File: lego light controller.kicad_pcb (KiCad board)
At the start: 2 copper layers, 31.8 x 31.8 mm, 29 parts, among them J1 Conn_01x02, J2 Conn_01x02, J3 Conn_01x02, J4 Conn_01x03, J5 Conn_01x03, J7 Conn_01x06_Pin, P1 USB_C_Plug_USB2.0, Q1 BC847W, Q2 BC847W, Q3 BC847W, U1 ATSAMD11C14A-SS, U2 AMS1117-3.3

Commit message: clean up pcb
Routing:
- net GND: track 2.35 -> 0.84 mm
- net /USB_N: track 12.6 -> 11.2 mm
- net /USB_P: track 9.55 -> 8.87 mm
- net Net-(J3-Pin_2): track 2.72 -> 2.09 mm
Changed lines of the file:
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@@
         (effects (font (size 1 1) (thickness 0.15)) (justify mirror))
     )
-    (fp_text value "10k" (at 0 1.43 90) (layer "F.Fab")
+    (fp_text value "10k" (at 0 1.43 90) (layer "F.Fab") hide
         (effects (font (size 1 1) (thickness 0.15)))
     )
@@
         (effects (font (size 1 1) (thickness 0.15)) (justify mirror))
     )
-    (fp_text value "1k" (at 0 1.43 90) (layer "F.Fab")
+    (fp_text value "1k" (at 0 1.43 90) (layer "F.Fab") hide
         (effects (font (size 1 1) (thickness 0.15)))
     )
@@
         (effects (font (size 1 1) (thickness 0.15)) (justify mirror))
     )
-    (fp_text value "100n" (at 40.94 0.35 90) (layer "F.Fab")
+    (fp_text value "100n" (at 40.94 0.35 90) (layer "F.Fab") hide
         (effects (font (size 1 1) (thickness 0.15)))
     )
@@
     (property "ki_keywords" "R res resistor")
     (attr smd)
-    (fp_text reference "R12" (at 2.2 0.15) (layer "B.SilkS")
+    (fp_text reference "R12" (at 1.95 1.15) (layer "B.SilkS")
         (effects (font (size 1 1) (thickness 0.15)) (justify mirror))
     )
@@
   )
   (segment (start 186 88.62) (end 186 89.465) (width 0.25) (layer "F.Cu") (net 1))
-  (segment (start 186 89.465) (end 185.625 89.84) (width 0.25) (layer "F.Cu") (net 1))
   (via (at 204.3 87.3) (size 0.8) (drill 0.4) (layers "F.Cu" "B.Cu") (free) (net 1))
   (via (at 194.7 89.9) (size 0.8) (drill 0.4) (layers "F.Cu" "B.Cu") (free) (net 1))
@@
   (via (at 187.2 84.6) (size 0.8) (drill 0.4) (layers "F.Cu" "B.Cu") (free) (net 1))
   (via (at 181.3 95.2) (size 0.8) (drill 0.4) (layers "F.Cu" "B.Cu") (free) (net 1))
-  (segment (start 185.771142 80.698712) (end 185.771142 81.671142) (width 0.25) (layer "B.Cu") (net 1))
   (segment (start 195.05 87.85) (end 195.27 87.63) (width 0.25) (layer "F.Cu") (net 2))
   (segment (start 188.45 88.9) (end 191.15 88.9) (width 0.25) (layer "F.Cu") (net 2))
   (segment (start 195.9 87.8) (end 195.85 87.85) (width 0.25) (layer "F.Cu") (net 2))
-  (segment (start 188.4 88.85) (end 188.45 88.9) (width 0.25) (layer "F.Cu") (net 2))
   (segment (start 190.1 92.2) (end 188.4 90.5) (width 0.25) (layer "F.Cu") (net 2))
   (segment (start 191.35 88.7) (end 194.2 88.7) (width 0.25) (layer "F.Cu") (net 2))
@@
   (segment (start 185.329594 87.87) (end 185.179594 87.72) (width 0.25) (layer "F.Cu") (net 3))
   (segment (start 185.4 83.05) (end 185.9 83.05) (width 0.25) (layer "F.Cu") (net 3))
-  (segment (start 185.9 87.75) (end 185.78 87.87) (width 0.25) (layer "F.Cu") (net 3))
   (segment (start 183.7 87.9) (end 183.7 84.75) (width 0.25) (layer "F.Cu") (net 3))
   (segment (start 190.7 96.7) (end 191.45 95.95) (width 0.5) (layer "F.Cu") (net 3))
   (segment (start 209.975 88) (end 208.475 86.5) (width 0.5) (layer "F.Cu") (net 3))
   (segment (start 209.5 96.7) (end 209.975 96.225) (width 0.5) (layer "F.Cu") (net 3))
-  (segment (start 204.96 84.94) (end 205.02 85) (width 0.5) (layer "B.Cu") (net 3))
   (segment (start 204.96 81.8) (end 204.96 84.94) (width 0.5) (layer "B.Cu") (net 3))
   (segment (start 205.1 89.2) (end 206.335 89.2) (width 0.25) (layer "F.Cu") (net 4))
   (segment (start 206.335 89.2) (end 207.535 88) (width 0.25) (layer "F.Cu") (net 4))
-  (segment (start 205 89.1) (end 205.1 89.2) (width 0.25) (layer "F.Cu") (net 4))
   (segment (start 205.05 91.8) (end 206.735 91.8) (width 0.25) (layer "F.Cu") (net 5))
-  (segment (start 205 91.75) (end 205.05 91.8) (width 0.25) (layer "F.Cu") (net 5))
   (segment (start 206.735 91.8) (end 207.535 91) (width 0.25) (layer "F.Cu") (net 5))
-  (segment (start 207.085 94.45) (end 207.535 94) (width 0.25) (layer "F.Cu") (net 6))
   (segment (start 205 94.45) (end 207.085 94.45) (width 0.25) (layer "F.Cu") (net 6))
   (segment (start 203.725 83.6) (end 206.16 83.6) (width 0.25) (layer "F.Cu") (net 7))
@@
   (segment (start 186 83.77) (end 187.43 83.77) (width 0.25) (layer "F.Cu") (net 10))
   (segment (start 187.43 83.77) (end 188.655 82.545) (width 0.25) (layer "F.Cu") (net 10))
-  (segment (start 188.655 82.545) (end 188.655 82.32) (width 0.25) (layer "F.Cu") (net 10))
   (segment (start 202.1 88) (end 202.1 90.6) (width 0.25) (layer "F.Cu") (net 11))
   (segment (start 201.525 87.425) (end 202.1 88) (width 0.25) (layer "F.Cu") (net 11))
@@
   (segment (start 185.43 91.87) (end 186.465 91.87) (width 0.25) (layer "F.Cu") (net 12))
   (segment (start 185.3 92) (end 185.43 91.87) (width 0.25) (layer "F.Cu") (net 12))
-  (segment (start 186.465 91.87) (end 186.465 91.635) (width 0.25) (layer "F.Cu") (net 12))
   (segment (start 185.974975 86.744975) (end 186 86.77) (width 0.25) (layer "F.Cu") (net 12))
   (via (at 184.555025 86.744975) (size 0.8) (drill 0.4) (layers "F.Cu" "B.Cu") (net 12))
@@
   (segment (start 189.774695 81.8) (end 196.195 81.8) (width 0.25) (layer "B.Cu") (net 23))
   (segment (start 190.19 87.6) (end 189.275 86.685) (width 0.25) (layer "B.Cu") (net 23))
-  (segment (start 186 86.27) (end 186.735 86.27) (width 0.2) (layer "F.Cu") (net 25))
   (segment (start 184.8 85.1) (end 185.13 84.77) (width 0.2) (layer "F.Cu") (net 25))
   (segment (start 186.775001 86.245) (end 186.750001 86.27) (width 0.2) (layer "F.Cu") (net 25))
-  (segment (start 191.46 86.175) (end 191.46 85.5) (width 0.2) (layer "F.Cu") (net 25))
-  (segment (start 186.750001 86.27) (end 186 86.27) (width 0.2) (layer "F.Cu") (net 25))
+  (segment (start 186 86.27) (end 186.750001 86.27) (width 0.2) (layer "F.Cu") (net 25))
   (segment (start 191.87 85.09) (end 191.87 84.7882) (width 0.2) (layer "F.Cu") (net 25))
   (segment (start 187.3732 86.245) (end 186.775001 86.245) (width 0.2) (layer "F.Cu") (net 25))
@@
   (segment (start 187.1868 85.795) (end 186.775001 85.795) (width 0.2) (layer "F.Cu") (net 26))
   (segment (start 186.775001 85.795) (end 186.750001 85.77) (width 0.2) (layer "F.Cu") (net 26))
-  (segment (start 192.73 86.175) (end 192.73 85.5) (width 0.2) (layer "F.Cu") (net 26))
   (segment (start 191.7432 84.025) (end 188.9568 84.025) (width 0.2) (layer "F.Cu") (net 26))
   (segment (start 192.32 85.09) (end 192.32 84.6018) (width 0.2) (layer "F.Cu") (net 26))

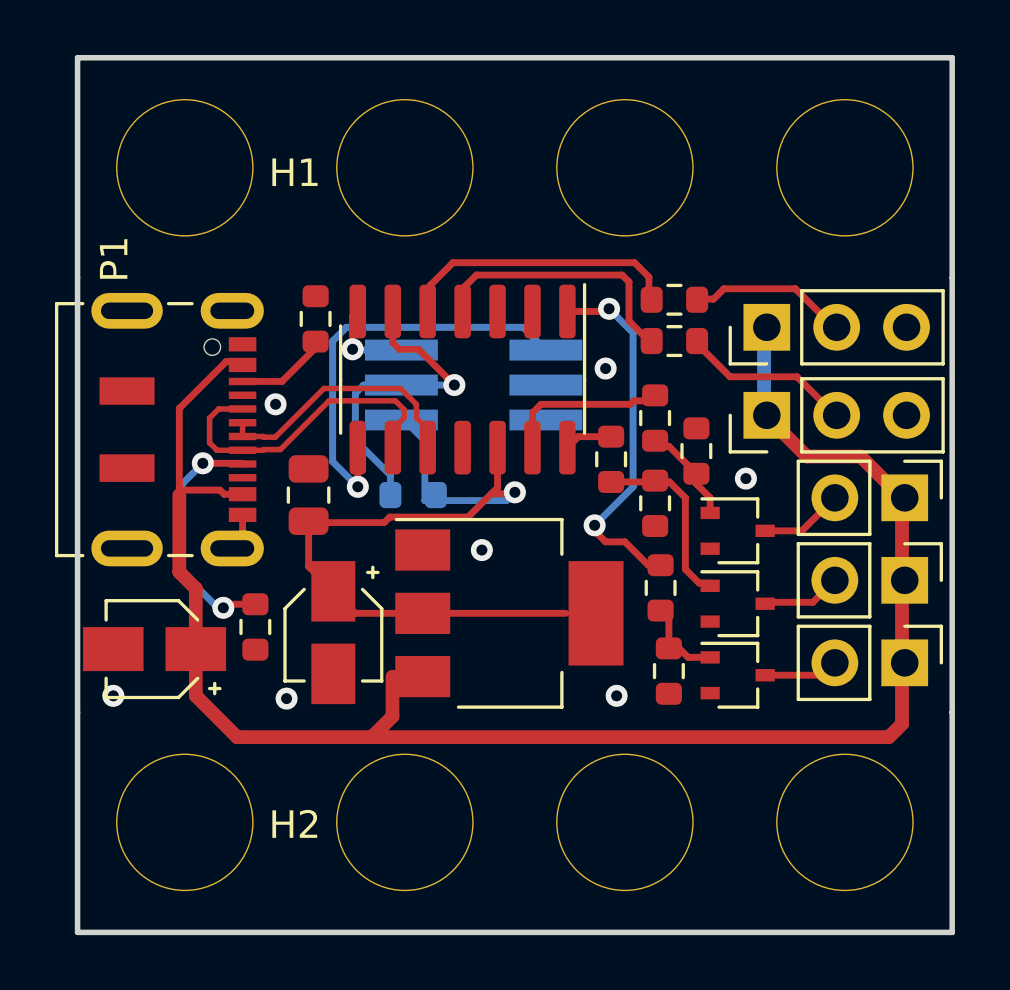
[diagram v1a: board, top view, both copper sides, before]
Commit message: fix trace to moved component
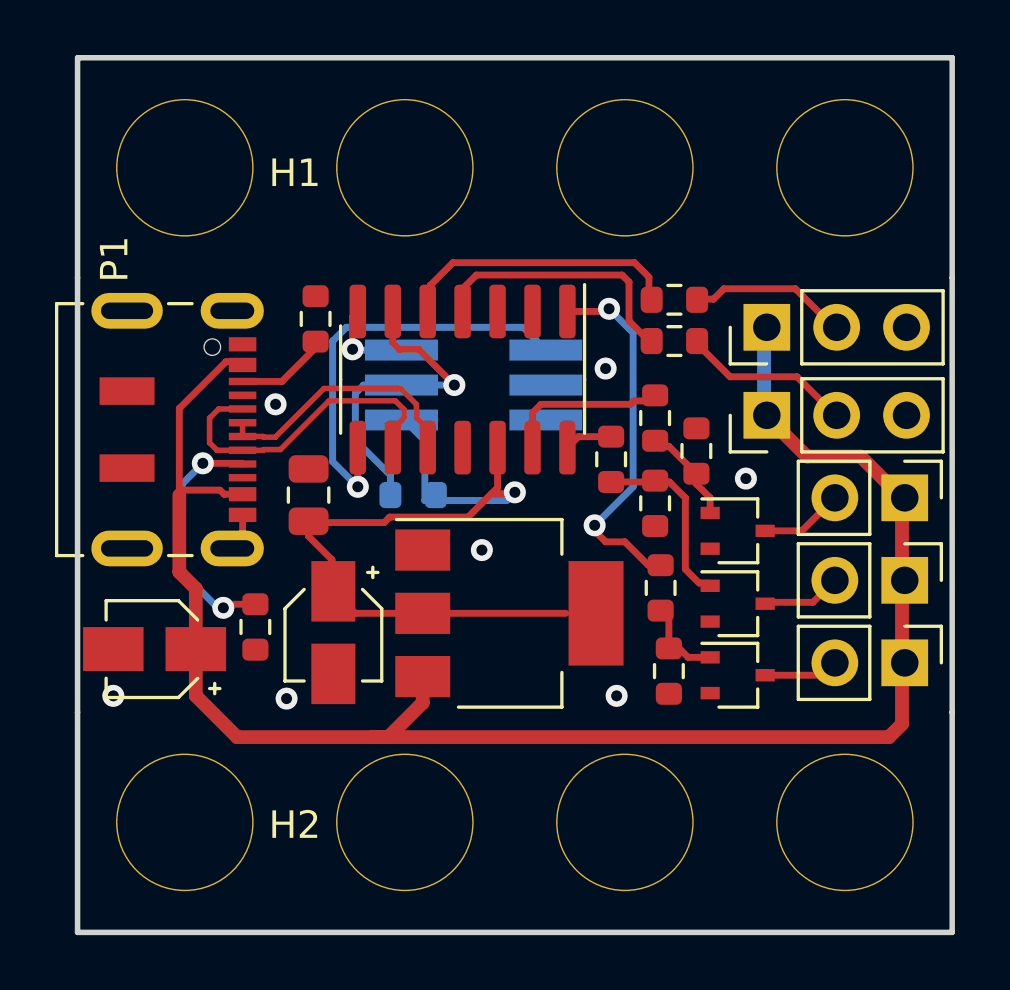
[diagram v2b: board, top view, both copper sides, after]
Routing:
- net +5V: track 62.4 -> 63.2 mm
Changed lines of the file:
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@@
   (segment (start 188.45 88.9) (end 191.15 88.9) (width 0.25) (layer "F.Cu") (net 2))
   (segment (start 195.9 87.8) (end 195.85 87.85) (width 0.25) (layer "F.Cu") (net 2))
-  (segment (start 190.1 92.2) (end 188.4 90.5) (width 0.25) (layer "F.Cu") (net 2))
+  (segment (start 189.25 90.25) (end 188.4 89.4) (width 0.25) (layer "F.Cu") (net 2))
+  (segment (start 197.75 92.2) (end 190.1 92.2) (width 0.25) (layer "F.Cu") (net 2))
+  (segment (start 190.1 92.2) (end 189.25 91.35) (width 0.25) (layer "F.Cu") (net 2))
+  (segment (start 189.25 91.35) (end 189.25 90.25) (width 0.25) (layer "F.Cu") (net 2))
   (segment (start 191.35 88.7) (end 194.2 88.7) (width 0.25) (layer "F.Cu") (net 2))
   (segment (start 191.15 88.9) (end 191.35 88.7) (width 0.25) (layer "F.Cu") (net 2))
-  (segment (start 197.75 92.2) (end 190.1 92.2) (width 0.25) (layer "F.Cu") (net 2))
-  (segment (start 188.4 90.5) (end 188.4 88.85) (width 0.25) (layer "F.Cu") (net 2))
+  (segment (start 188.4 89.4) (end 188.4 88.85) (width 0.25) (layer "F.Cu") (net 2))
   (segment (start 195.27 87.63) (end 195.27 86.175) (width 0.25) (layer "F.Cu") (net 2))
   (segment (start 195.85 87.85) (end 195.05 87.85) (width 0.25) (layer "F.Cu") (net 2))
@@
   (segment (start 209.975 96.225) (end 209.975 94) (width 0.5) (layer "F.Cu") (net 3))
   (segment (start 184.3 95.2) (end 184.3 91.3) (width 0.5) (layer "F.Cu") (net 3))
+  (segment (start 191.3 96.7) (end 192.55 95.45) (width 0.5) (layer "F.Cu") (net 3))
   (segment (start 209.975 91) (end 209.975 88) (width 0.5) (layer "F.Cu") (net 3))
   (segment (start 185.8 96.7) (end 184.3 95.2) (width 0.5) (layer "F.Cu") (net 3))
@@
   (segment (start 190.7 96.7) (end 209.5 96.7) (width 0.5) (layer "F.Cu") (net 3))
   (segment (start 206.52 86.5) (end 205.02 85) (width 0.5) (layer "F.Cu") (net 3))
-  (segment (start 191.45 95.95) (end 191.45 94.5) (width 0.5) (layer "F.Cu") (net 3))
+  (segment (start 190.7 96.7) (end 191.3 96.7) (width 0.5) (layer "F.Cu") (net 3))
   (segment (start 185.179594 87.72) (end 183.88 87.72) (width 0.25) (layer "F.Cu") (net 3))
   (segment (start 185.329594 87.87) (end 185.179594 87.72) (width 0.25) (layer "F.Cu") (net 3))
   (segment (start 185.4 83.05) (end 185.9 83.05) (width 0.25) (layer "F.Cu") (net 3))
   (segment (start 183.7 87.9) (end 183.7 84.75) (width 0.25) (layer "F.Cu") (net 3))
-  (segment (start 190.7 96.7) (end 191.45 95.95) (width 0.5) (layer "F.Cu") (net 3))
   (segment (start 209.975 88) (end 208.475 86.5) (width 0.5) (layer "F.Cu") (net 3))
+  (segment (start 192.55 95.45) (end 192.55 94.5) (width 0.5) (layer "F.Cu") (net 3))
   (segment (start 209.5 96.7) (end 209.975 96.225) (width 0.5) (layer "F.Cu") (net 3))
   (segment (start 204.96 81.8) (end 204.96 84.94) (width 0.5) (layer "B.Cu") (net 3))

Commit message: fix track to 3v3 outpu
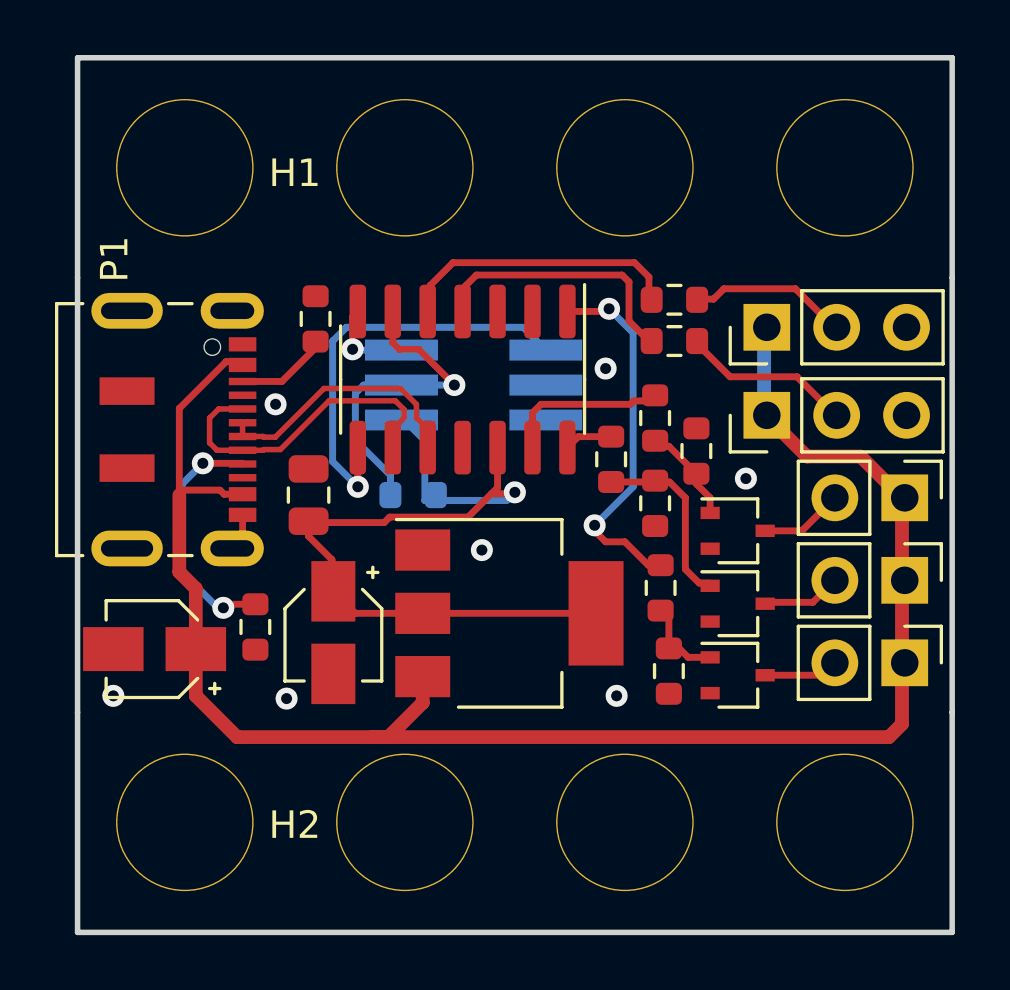
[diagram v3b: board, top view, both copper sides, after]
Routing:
- net +3V3: track 28.0 -> 29.1 mm
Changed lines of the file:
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@@
   (segment (start 195.05 87.85) (end 195.27 87.63) (width 0.25) (layer "F.Cu") (net 2))
   (segment (start 188.45 88.9) (end 191.15 88.9) (width 0.25) (layer "F.Cu") (net 2))
+  (segment (start 190.1 92.2) (end 189.25 91.35) (width 0.25) (layer "F.Cu") (net 2))
   (segment (start 195.9 87.8) (end 195.85 87.85) (width 0.25) (layer "F.Cu") (net 2))
+  (segment (start 198.85 92.2) (end 190.1 92.2) (width 0.25) (layer "F.Cu") (net 2))
   (segment (start 189.25 90.25) (end 188.4 89.4) (width 0.25) (layer "F.Cu") (net 2))
-  (segment (start 197.75 92.2) (end 190.1 92.2) (width 0.25) (layer "F.Cu") (net 2))
-  (segment (start 190.1 92.2) (end 189.25 91.35) (width 0.25) (layer "F.Cu") (net 2))
   (segment (start 189.25 91.35) (end 189.25 90.25) (width 0.25) (layer "F.Cu") (net 2))
+  (segment (start 188.4 89.4) (end 188.4 88.85) (width 0.25) (layer "F.Cu") (net 2))
   (segment (start 191.35 88.7) (end 194.2 88.7) (width 0.25) (layer "F.Cu") (net 2))
   (segment (start 191.15 88.9) (end 191.35 88.7) (width 0.25) (layer "F.Cu") (net 2))
-  (segment (start 188.4 89.4) (end 188.4 88.85) (width 0.25) (layer "F.Cu") (net 2))
   (segment (start 195.27 87.63) (end 195.27 86.175) (width 0.25) (layer "F.Cu") (net 2))
   (segment (start 195.85 87.85) (end 195.05 87.85) (width 0.25) (layer "F.Cu") (net 2))

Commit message: update footprints and redo layout
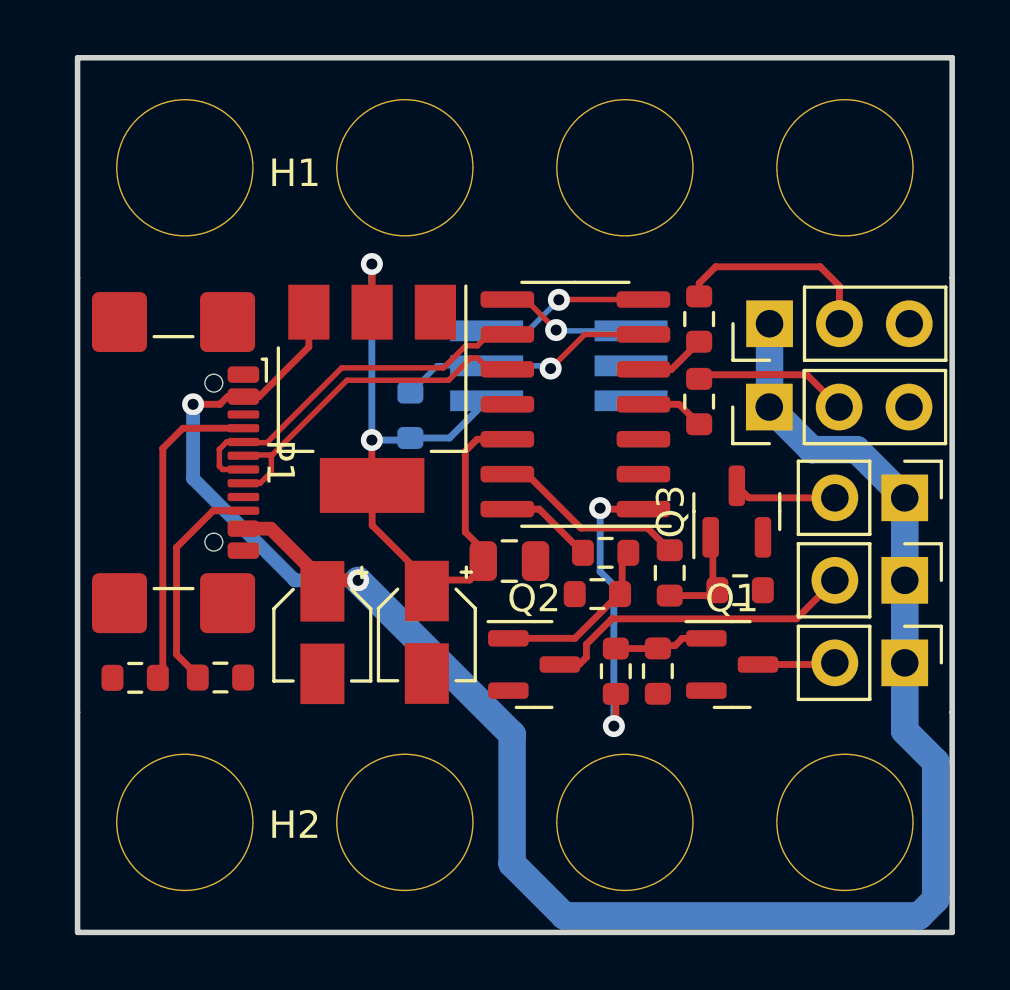
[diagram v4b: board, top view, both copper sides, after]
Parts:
- P1: footprint Connector_USB:USB_C_Receptacle_JAE_DX07S016JA1R1500 -> Connector_USB:USB_C_Receptacle_GCT_USB4110
- Q1, Q2, Q3: footprint Package_TO_SOT_SMD:SOT-323_SC-70 -> Package_TO_SOT_SMD:SOT-23
- moved R1 14.6 mm to (182.1, 94.5), turned to 180 degrees
- moved U2 9.26 mm to (190.7, 84.4), turned to -90 degrees
- moved Q2 7.72 mm to (196.6, 94.1)
- moved C3 7.68 mm to (195.7, 90.3), turned to 180 degrees
- moved C1 6.13 mm to (188.9, 92.9), turned to -90 degrees
- moved R9 5.65 mm to (201.5, 90.7)
- moved R4 5.30 mm to (204.1, 91.4), turned to 180 degrees
- moved U1 4.20 mm to (198.1, 84.6), turned to 180 degrees
- moved R5 3.91 mm to (198.9, 91.5), turned to 0 degrees
- moved R7 3.44 mm to (199.6, 94.3), turned to -90 degrees
- moved R8 3.41 mm to (199.2, 90.0), turned to 180 degrees
- moved C2 3.40 mm to (192.7, 92.9)
- moved J7 3.18 mm to (197.5, 83.2)
- moved R12 2.90 mm to (192.1, 85.0), turned to 90 degrees
- moved R10 2.38 mm to (202.6, 84.5), turned to -90 degrees
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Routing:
- net +5V: track 63.2 -> 75.0 mm, vias 0 -> 2
- net Net-(J7-Pin_4): track 15.4 -> 4.97 mm
- net Net-(J2-Pin_2): track 2.82 -> 11.5 mm
- net Net-(P1-CC1): track 3.16 -> 11.7 mm
- net /DL2: track 10.3 -> 2.44 mm
- net /DL1: track 9.59 -> 2.33 mm
- net /USB_P: track 8.87 -> 13.0 mm
- net Net-(J7-Pin_3): track 3.24 -> 6.17 mm
- net /LED3: track 13.8 -> 10.9 mm
- net Net-(J7-Pin_2): track 12.1 -> 9.43 mm
- net /USB_N: track 11.2 -> 13.8 mm
- net Net-(J5-Pin_2): track 5.84 -> 7.48 mm
- net +3V3: track 29.1 -> 27.5 mm, vias 1 -> 2
- net /LED2: track 1.96 -> 3.41 mm
- net /LED1: track 5.91 -> 7.05 mm
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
